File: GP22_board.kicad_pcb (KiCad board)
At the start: 4 copper layers, 100 x 100 mm, 117 parts, among them CON1 5V power input, IC1 ATMEGA328P-A, P1 TTLOut1, P10 S- DC/AC, P11 S+ DC/AC, P12 S- DC/AC, P13 TTLOut2, P14 TTLOut3, P15 PWR_SEL, P16 FILT_SEL, P2 SineInput, P3 TTLInput, P4 USB_OTG, P5 ICSP, P6 STInput, P7 S+ DC/AC, P8 S- DC/AC, P9 S+ DC/AC, SW1 START, SW2 STOP1, SW3 STOP2, U1 RS 252-210, U10 XC6206, U11 ISO7242, U12 FT232RL, U2 GP22, U3 LTC6957-4, U4 ISO3088, U5 IDT49FCT, U6 LD1117S33TR, U7 MC74VHC1GT04, U8 SN74LV8154, U9 SC74HC165N, X1 TSX-3225 X1E0000210013, Y1 4MHz, Y2 32.768 kHz

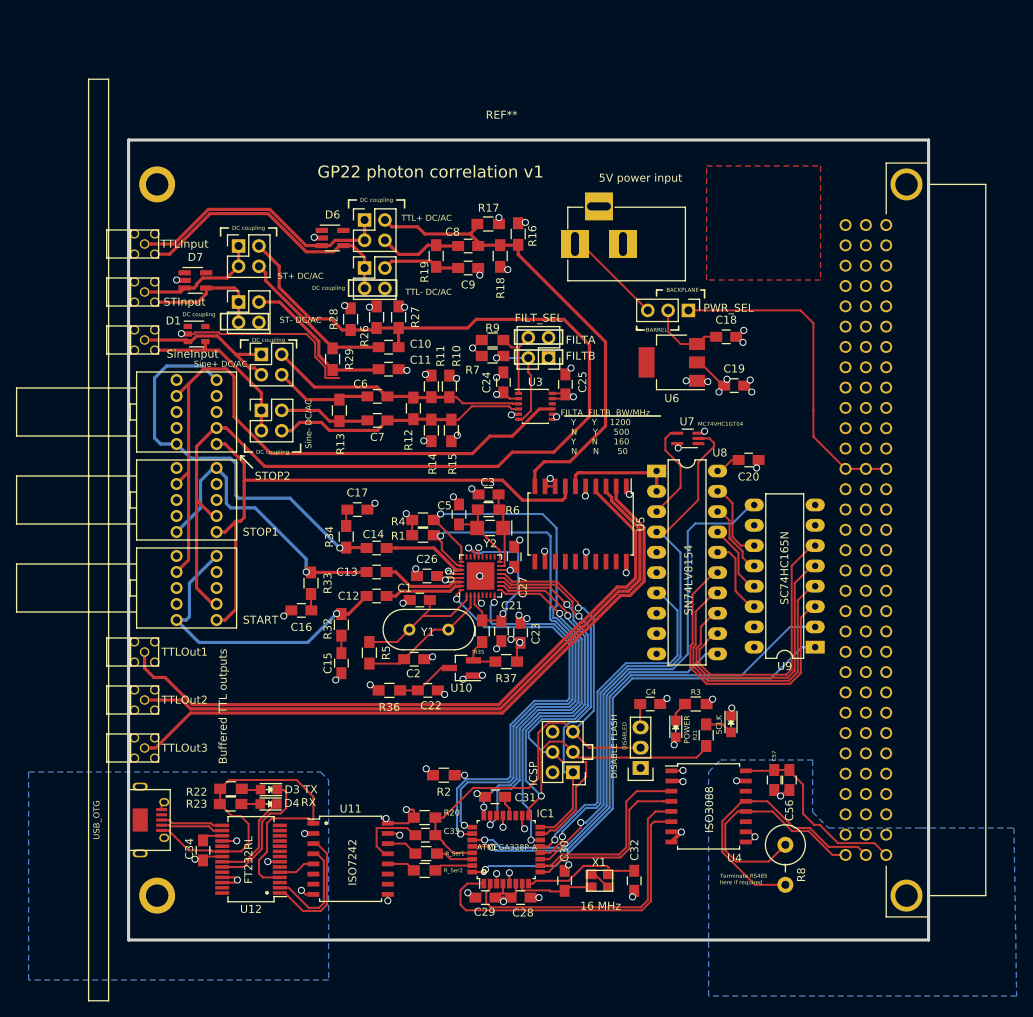
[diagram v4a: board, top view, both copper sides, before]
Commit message: Flood the top and bottom
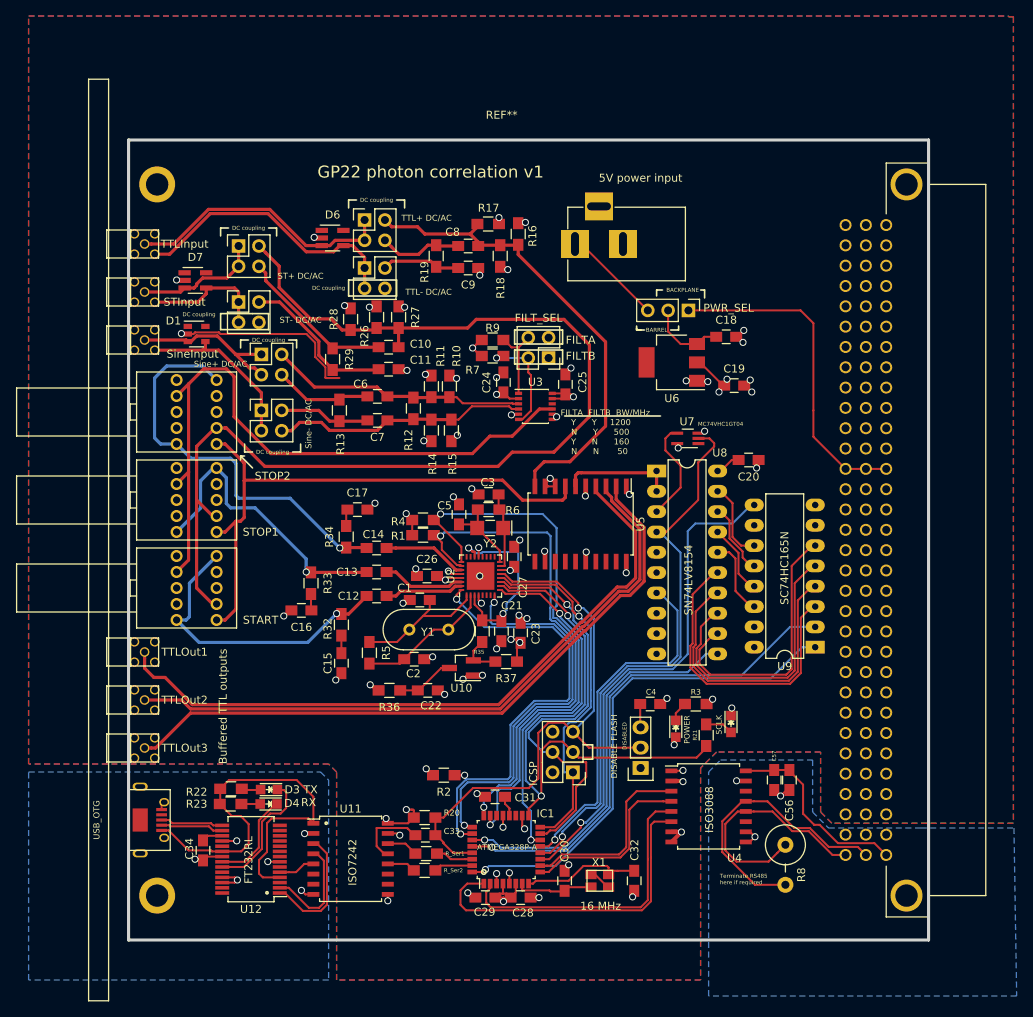
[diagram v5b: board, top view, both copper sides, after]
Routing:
- added copper zone on B.Cu, net GND
- added copper zone on F.Cu, net GND
- removed copper zone on F.Cu, net (none)
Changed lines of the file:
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@@
   (page A4)
   (layers
-    (0 F.Cu signal)
-    (1 In1.Cu signal hide)
-    (2 In2.Cu signal hide)
-    (31 B.Cu signal)
+    (0 F.Cu signal hide)
+    (1 In1.Cu signal)
+    (2 In2.Cu signal)
+    (31 B.Cu signal hide)
     (32 B.Adhes user)
     (33 F.Adhes user)
@@
     (visible_elements 7FFF6F7F)
     (pcbplotparams
-      (layerselection 0x010f0_80000007)
+      (layerselection 0x010fc_80000007)
       (usegerberextensions true)
       (excludeedgelayer true)
@@
       (pts
         (xy 191 114) (xy 191 138) (xy 190 138) (xy 190 115) (xy 189 114)
-        (xy 158 114) (xy 158 113) (xy 190 113) (xy 191 114)
+        (xy 158 114) (xy 158 113) (xy 190 113)
       )
     )
@@
     )
   )
-  (zone (net 0) (net_name "") (layer F.Cu) (hatch edge 0.508)
+  (zone (net 32) (net_name GND) (layer F.Cu) (hatch edge 0.508)
+    (connect_pads (clearance 0.508))
+    (min_thickness 0.254)
+    (fill yes (arc_segments 16) (thermal_gap 0.508) (thermal_bridge_width 0.508))
+    (polygon
+      (pts
+        (xy 275 19.6) (xy 275.6 19.6) (xy 275.6 120.4) (xy 252.9 120.4) (xy 251.5 119)
+        (xy 251.5 111.5) (xy 238.5 111.5) (xy 236.5 113.5) (xy 236.5 140) (xy 191 140)
+        (xy 191 114) (xy 190 113) (xy 152.5 113) (xy 152.5 19.5) (xy 275 19.5)
+      )
+    )
+  )
+  (zone (net 32) (net_name GND) (layer B.Cu) (hatch edge 0.508)
     (connect_pads (clearance 0.508))
     (min_thickness 0.254)
@@
     (polygon
       (pts
-        (xy 237.25 38.25) (xy 251.5 38.25) (xy 251.5 52.5) (xy 237.25 52.5)
+        (xy 275 19.6) (xy 275.6 19.6) (xy 275.6 120.4) (xy 252.9 120.4) (xy 251.5 119)
+        (xy 251.5 111.5) (xy 238.5 111.5) (xy 236.5 113.5) (xy 236.5 140) (xy 191 140)
+        (xy 191 114) (xy 190 113) (xy 152.5 113) (xy 152.5 19.5) (xy 275 19.5)
       )
     )

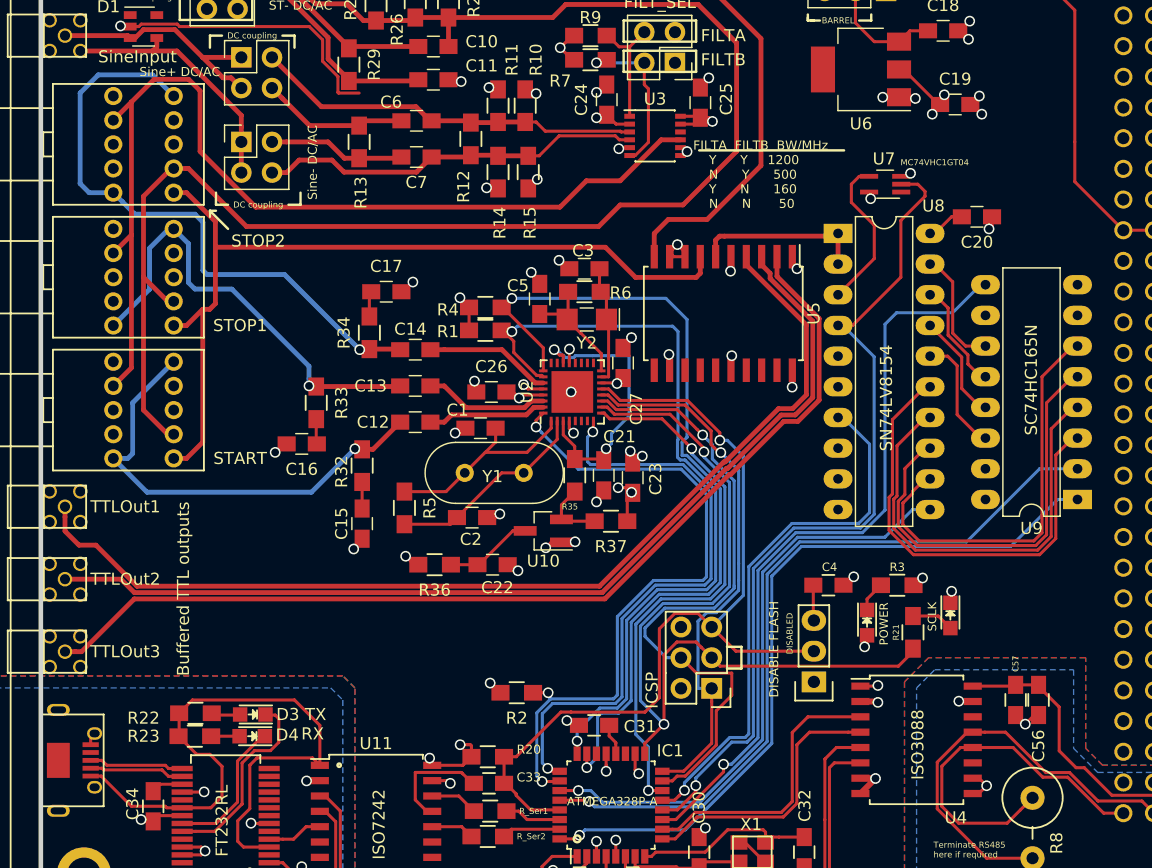
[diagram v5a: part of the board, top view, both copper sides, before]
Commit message: Swap plane order and route power by bottom pour, for EMC and ground-inductance considerations
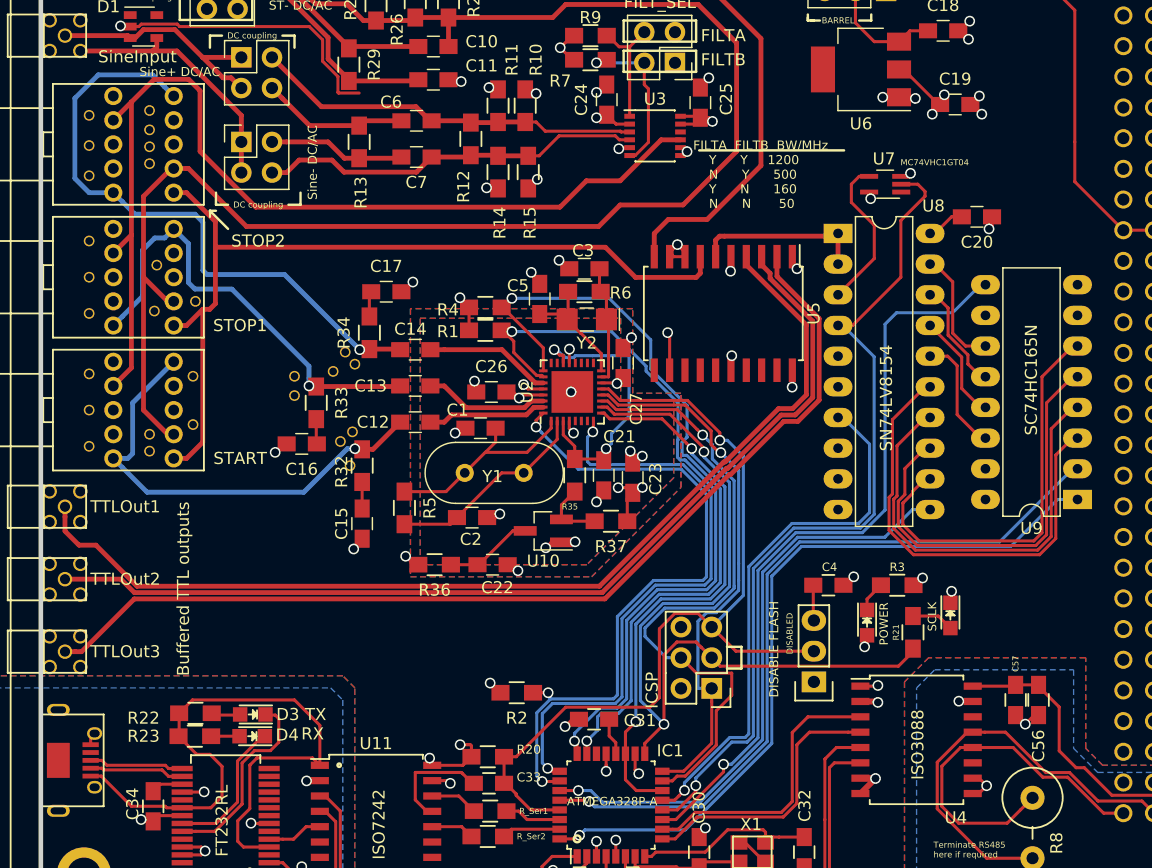
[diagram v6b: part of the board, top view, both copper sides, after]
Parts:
- added VIA**: ViaHack, Custom:ViaHack, F.Cu at (169.0, 66.6)
- added VIA**: ViaHack, Custom:ViaHack, F.Cu at (174.0, 94.4)
- added VIA**: ViaHack, Custom:ViaHack, F.Cu at (174.0, 93.0)
- added VIA**: ViaHack, Custom:ViaHack, F.Cu at (177.6, 92.2)
- added VIA**: ViaHack, Custom:ViaHack, F.Cu at (177.6, 88.2)
- added VIA**: ViaHack, Custom:ViaHack, F.Cu at (177.8, 82.0)
- added VIA**: ViaHack, Custom:ViaHack, F.Cu at (174.6, 79.0)
- added VIA**: ViaHack, Custom:ViaHack, F.Cu at (174.4, 82.8)
- added VIA**: ViaHack, Custom:ViaHack, F.Cu at (174.0, 66.2)
- added VIA**: ViaHack, Custom:ViaHack, F.Cu at (174.0, 67.8)
- added VIA**: ViaHack, Custom:ViaHack, F.Cu at (174.0, 69.2)
- added VIA**: ViaHack, Custom:ViaHack, F.Cu at (169.0, 69.1)
- added VIA**: ViaHack, Custom:ViaHack, F.Cu at (174.0, 70.6)
- added VIA**: ViaHack, Custom:ViaHack, F.Cu at (190.6, 95.6)
- added VIA**: ViaHack, Custom:ViaHack, F.Cu at (190.8, 92.8)
- added VIA**: ViaHack, Custom:ViaHack, F.Cu at (189.8, 93.6)
- added VIA**: ViaHack, Custom:ViaHack, F.Cu at (190.2, 86.2)
- added VIA**: ViaHack, Custom:ViaHack, F.Cu at (191.0, 87.2)
- added VIA**: ViaHack, Custom:ViaHack, F.Cu at (189.2, 87.8)
- added VIA**: ViaHack, Custom:ViaHack, F.Cu at (186.0, 89.8)
- added VIA**: ViaHack, Custom:ViaHack, F.Cu at (186.0, 88.2)
- added VIA**: ViaHack, Custom:ViaHack, F.Cu at (169.0, 71.6)
- added VIA**: ViaHack, Custom:ViaHack, F.Cu at (169.0, 77.0)
- added VIA**: ViaHack, Custom:ViaHack, F.Cu at (169.0, 80.0)
- added VIA**: ViaHack, Custom:ViaHack, F.Cu at (169.0, 83.0)
- added VIA**: ViaHack, Custom:ViaHack, F.Cu at (169.0, 94.0)
- added VIA**: ViaHack, Custom:ViaHack, F.Cu at (169.0, 91.0)
- added VIA**: ViaHack, Custom:ViaHack, F.Cu at (169.0, 88.0)
- moved C31 0.50 mm to (210.8, 116.6)
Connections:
- IC1 pad 19: (no net) -> /GP22_CS
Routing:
- net /GP22_EN_STOP2: track 70.8 -> 65.8 mm
- net /GP22_EN_STOP1: track 65.2 -> 61.8 mm
- net +3V3: track 53.0 -> 54.8 mm
- net /GP22_CS: track 45.2 -> 46.5 mm
- net /GP22_VCC: track 9.41 -> 10.3 mm
- net GND: track 132.0 -> 132.8 mm
- net Net-(C31-Pad1): track 2.58 -> 3.08 mm
- added copper zone on B.Cu, net +3V3
- added copper zone on F.Cu, net +3V3
- added copper zone on B.Cu, net /GP22_VCC
- added copper zone on In2.Cu, net GND
- removed copper zone on In2.Cu, net +3V3
- removed copper zone on In2.Cu, net /GP22_VCC
- removed copper zone on B.Cu, net GND
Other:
- board text added: "A note on planes: This is a four layer board. The internal planes are both connected to ground: this ensures that signals on both the top and bottom layers have a low-impedance return path. Placing GND vias close to points where RF signals switch from layer 1 -> 4 allows the return current to switch internal plane, reducing impedance again. The top and bottom layers supply power via a copper pour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"
- board text removed: "3-5V needs to be supplied to the microprocessor. A ground plane as shown is highly recommended to reduce EMI and signal inductance."

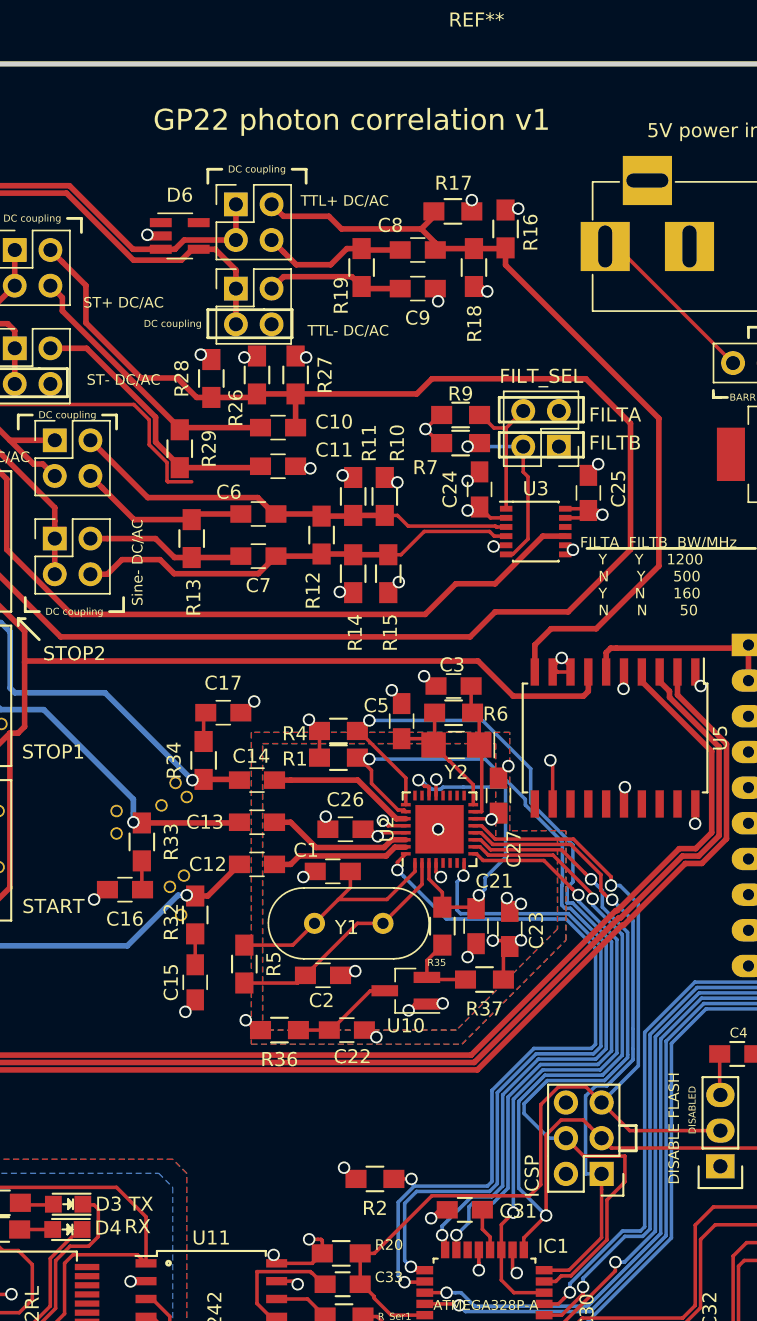
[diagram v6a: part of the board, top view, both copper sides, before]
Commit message: Add soldermask to via hack, label board, gerbers
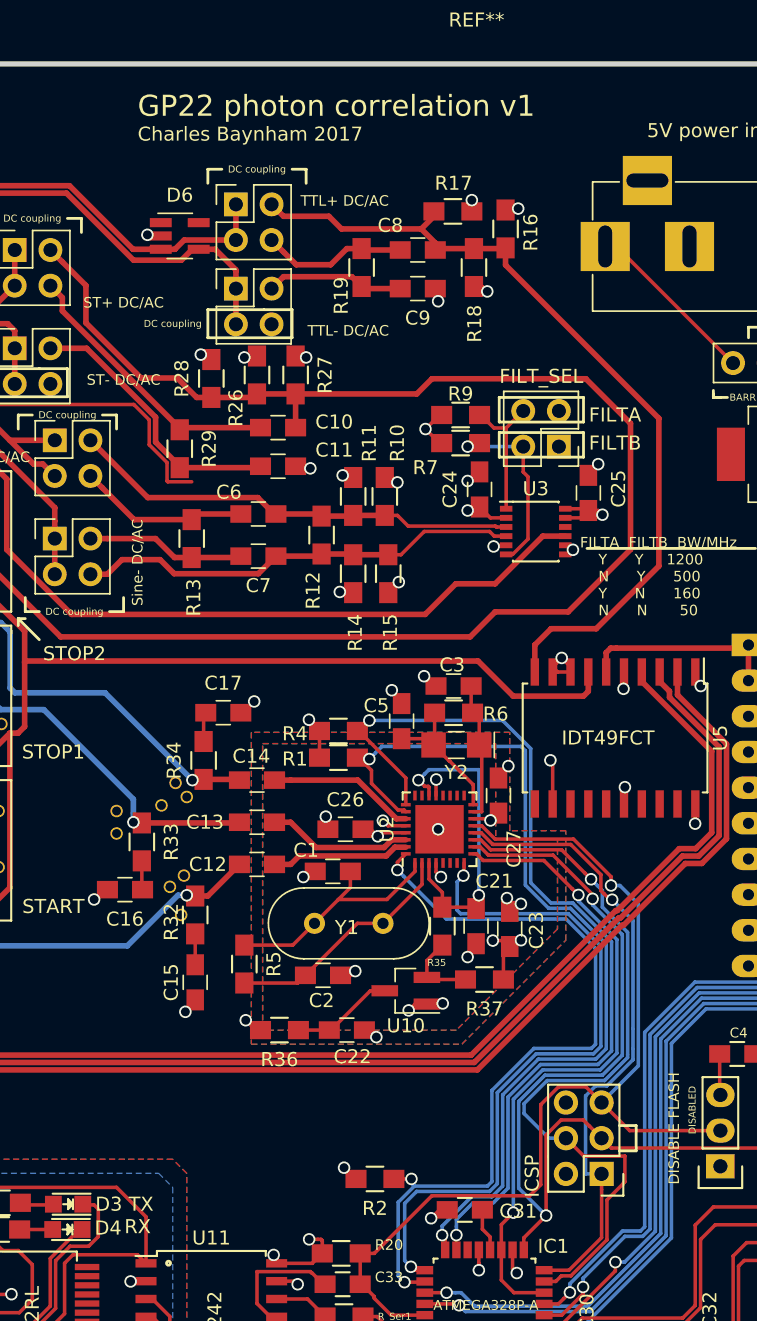
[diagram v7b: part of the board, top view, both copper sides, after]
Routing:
- net /GP22_EN_STOP1: track 61.8 -> 65.2 mm
- net /GP22_VIO: track 23.7 -> 22.4 mm
- net /GP22_EN_STOP2: track 65.8 -> 66.9 mm
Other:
- board text added: "Charles Baynham 2017"
